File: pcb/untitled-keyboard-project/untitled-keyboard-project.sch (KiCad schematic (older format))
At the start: 64 parts, among them J1 USB_mini_micro_B, K1 KEYSW, K10 KEYSW, K11 KEYSW, K12 KEYSW, K13 KEYSW, K14 KEYSW, K15 KEYSW, K16 KEYSW, K17 KEYSW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

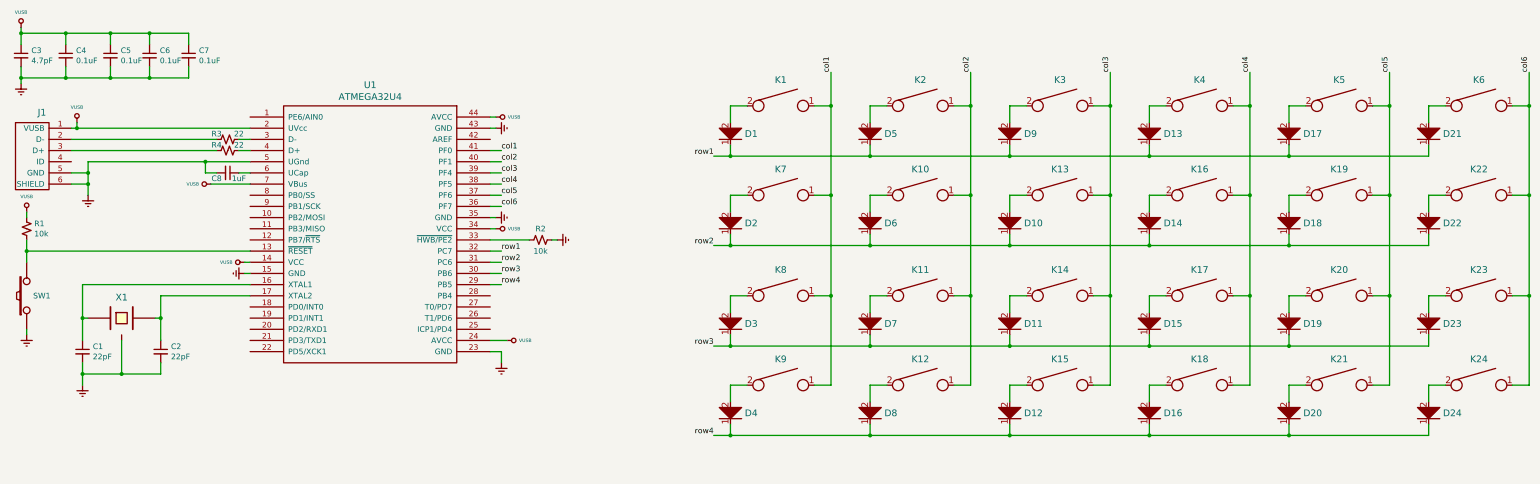
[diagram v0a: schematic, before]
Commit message: Update 12/23/19 00:05
Reorganized KiCAD project. Created PCB file and started laying out components.
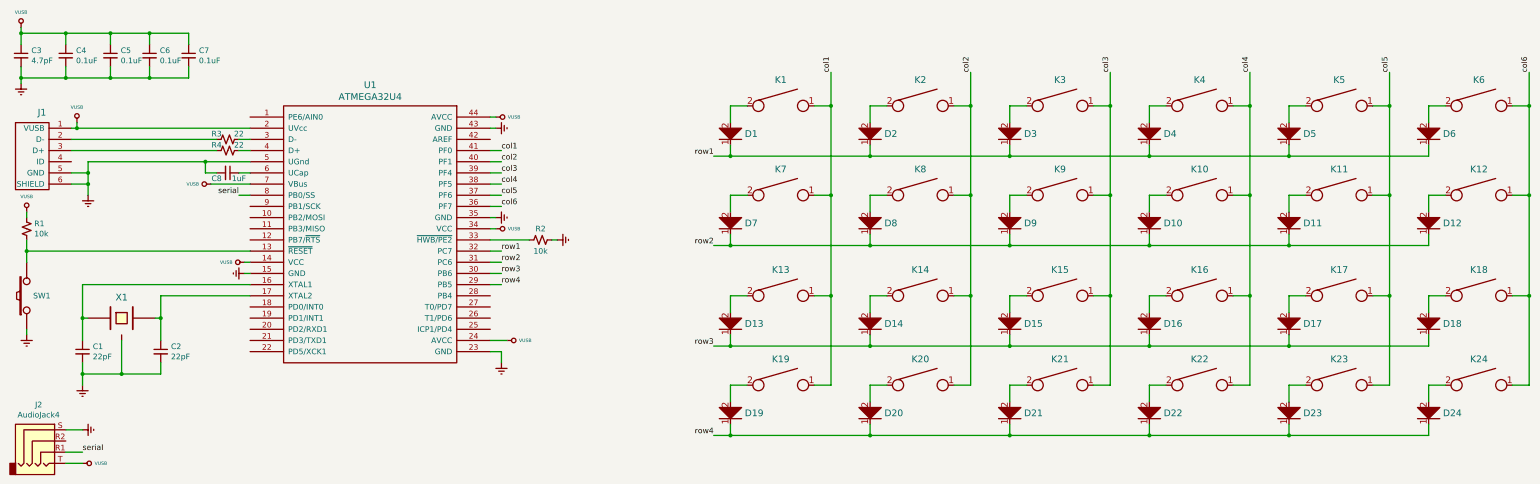
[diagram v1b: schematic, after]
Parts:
- added J2: AudioJack4, Connector_Audio:Jack_3.5mm_PJ320E_Horizontal, symbol Connector:AudioJack4
- D1, D24: footprint (none) -> Diode_SMD:D_0603_1608Metric
- D10: renamed from D14; footprint (none) -> Diode_SMD:D_0603_1608Metric
- D11: renamed from D18; footprint (none) -> Diode_SMD:D_0603_1608Metric
- D12: renamed from D22; footprint (none) -> Diode_SMD:D_0603_1608Metric
- D13: renamed from D3; footprint (none) -> Diode_SMD:D_0603_1608Metric
- D14: renamed from D7; footprint (none) -> Diode_SMD:D_0603_1608Metric
- D15: renamed from D11; footprint (none) -> Diode_SMD:D_0603_1608Metric
- D16: renamed from D15; footprint (none) -> Diode_SMD:D_0603_1608Metric
- D17: renamed from D19; footprint (none) -> Diode_SMD:D_0603_1608Metric
- D18: renamed from D23; footprint (none) -> Diode_SMD:D_0603_1608Metric
- D19: renamed from D4; footprint (none) -> Diode_SMD:D_0603_1608Metric
- D2: renamed from D5; footprint (none) -> Diode_SMD:D_0603_1608Metric
- D20: renamed from D8; footprint (none) -> Diode_SMD:D_0603_1608Metric
- D21: renamed from D12; footprint (none) -> Diode_SMD:D_0603_1608Metric
- D22: renamed from D16; footprint (none) -> Diode_SMD:D_0603_1608Metric
- D23: renamed from D20; footprint (none) -> Diode_SMD:D_0603_1608Metric
- D3: renamed from D9; footprint (none) -> Diode_SMD:D_0603_1608Metric
- D4: renamed from D13; footprint (none) -> Diode_SMD:D_0603_1608Metric
- D5: renamed from D17; footprint (none) -> Diode_SMD:D_0603_1608Metric
- D6: renamed from D21; footprint (none) -> Diode_SMD:D_0603_1608Metric
- D7: renamed from D2; footprint (none) -> Diode_SMD:D_0603_1608Metric
- D8: renamed from D6; footprint (none) -> Diode_SMD:D_0603_1608Metric
- D9: renamed from D10; footprint (none) -> Diode_SMD:D_0603_1608Metric
- J1: footprint (none) -> Connector_USB:USB_Micro-B_Molex-105017-0001
- K1, K2, K24, K3, K4, K5, K6, K7: footprint (none) -> Button_Switch_Keyboard:SW_Cherry_MX_1.00u_PCB
- K10: renamed from K16; footprint (none) -> Button_Switch_Keyboard:SW_Cherry_MX_1.00u_PCB
- K11: renamed from K19; footprint (none) -> Button_Switch_Keyboard:SW_Cherry_MX_1.00u_PCB
- K12: renamed from K22; footprint (none) -> Button_Switch_Keyboard:SW_Cherry_MX_1.00u_PCB
- K13: renamed from K8; footprint (none) -> Button_Switch_Keyboard:SW_Cherry_MX_1.00u_PCB
- K14: renamed from K11; footprint (none) -> Button_Switch_Keyboard:SW_Cherry_MX_1.00u_PCB
- K15: renamed from K14; footprint (none) -> Button_Switch_Keyboard:SW_Cherry_MX_1.00u_PCB
- K16: renamed from K17; footprint (none) -> Button_Switch_Keyboard:SW_Cherry_MX_1.00u_PCB
- K17: renamed from K20; footprint (none) -> Button_Switch_Keyboard:SW_Cherry_MX_1.00u_PCB
- K18: renamed from K23; footprint (none) -> Button_Switch_Keyboard:SW_Cherry_MX_1.00u_PCB
- K19: renamed from K9; footprint (none) -> Button_Switch_Keyboard:SW_Cherry_MX_1.00u_PCB
- K20: renamed from K12; footprint (none) -> Button_Switch_Keyboard:SW_Cherry_MX_1.00u_PCB
- K21: renamed from K15; footprint (none) -> Button_Switch_Keyboard:SW_Cherry_MX_1.00u_PCB
- K22: renamed from K18; footprint (none) -> Button_Switch_Keyboard:SW_Cherry_MX_1.00u_PCB
- K23: renamed from K21; footprint (none) -> Button_Switch_Keyboard:SW_Cherry_MX_1.00u_PCB
- K8: renamed from K10; footprint (none) -> Button_Switch_Keyboard:SW_Cherry_MX_1.00u_PCB
- K9: renamed from K13; footprint (none) -> Button_Switch_Keyboard:SW_Cherry_MX_1.00u_PCB
- X1: footprint (none) -> Crystal:Crystal_SMD_TXC_7M-4Pin_3.2x2.5mm
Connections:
- net GNDREF: now also J2.S
- net VUSB: now also J2.T
- net serial: now reaches U1.8 (PB0/SS)
- net serial: now also J2.R1

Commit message: Finished layout for Rev 0 board
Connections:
- net row1: now also U1.19 (PD1/INT1); no longer U1.32 (PC7)
- net row2: now also U1.20 (PD2/RXD1); no longer U1.31 (PC6)
- net row3: now also U1.21 (PD3/TXD1); no longer U1.30 (PB6)
- net row4: now also U1.22 (PD5/XCK1); no longer U1.29 (PB5)
- net reset: now reaches R1.1, SW1.2, U1.13 (~RESET)
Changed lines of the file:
@@
 	0    -1   -1   0
 $EndComp
-Wire Wire Line
-	3700 2800 1700 2800
-Wire Wire Line
-	1700 2800 1700 2900
 $Comp
 L power:GNDREF #PWR0108
@@
 Wire Wire Line
 	6450 2700 6400 2700
-Wire Wire Line
-	1700 2700 1700 2800
-Connection ~ 1700 2800
 $Comp
 L keyboard_parts:VUSB #PWR0110
@@
 Wire Wire Line
 	5850 2400 5950 2400
-Wire Wire Line
-	5850 2800 5950 2800
-Wire Wire Line
-	5850 2900 5950 2900
-Wire Wire Line
-	5850 3000 5950 3000
-Wire Wire Line
-	5850 3100 5950 3100
 Text Label 5950 2000 0    50   ~ 0
 col2
@@
 Text Label 5950 2400 0    50   ~ 0
 col6
-Text Label 5950 2800 0    50   ~ 0
-row1
-Text Label 5950 2900 0    50   ~ 0
-row2
-Text Label 5950 3000 0    50   ~ 0
-row3
-Text Label 5950 3100 0    50   ~ 0
-row4
 Text Label 7850 1950 2    50   ~ 0
 row1
@@
 	1    0    0    -1
 $EndComp
+Connection ~ 1700 2800
+Wire Wire Line
+	1700 2700 1700 2800
+Wire Wire Line
+	1700 2800 1700 2900
+Text Label 3600 2800 2    50   ~ 0
+reset
+Wire Wire Line
+	3700 2800 1700 2800
+Wire Wire Line
+	3700 3700 3600 3700
+Wire Wire Line
+	3700 3600 3600 3600
+Wire Wire Line
+	3700 3500 3600 3500
+Wire Wire Line
+	3700 3400 3600 3400
+Text Label 3600 3700 2    50   ~ 0
+row4
+Text Label 3600 3600 2    50   ~ 0
+row3
+Text Label 3600 3500 2    50   ~ 0
+row2
+Text Label 3600 3400 2    50   ~ 0
+row1
 $EndSCHEMATC

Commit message: Update 11/28/2020
Capacitor Value Change
File Cleanup
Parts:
- C1, C2: value 22pF -> 18pF
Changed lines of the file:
@@
 P 2200 3700
 F 0 "C1" H 2292 3746 50  0000 L CNN
-F 1 "22pF" H 2292 3655 50  0000 L CNN
+F 1 "18pF" H 2292 3655 50  0000 L CNN
 F 2 "Capacitor_SMD:C_0805_2012Metric" H 2200 3700 50  0001 C CNN
 F 3 "~" H 2200 3700 50  0001 C CNN
@@
 P 2900 3700
 F 0 "C2" H 2992 3746 50  0000 L CNN
-F 1 "22pF" H 2992 3655 50  0000 L CNN
+F 1 "18pF" H 2992 3655 50  0000 L CNN
 F 2 "Capacitor_SMD:C_0805_2012Metric" H 2900 3700 50  0001 C CNN
 F 3 "~" H 2900 3700 50  0001 C CNN
